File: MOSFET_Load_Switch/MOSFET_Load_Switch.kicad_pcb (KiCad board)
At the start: 4 copper layers, 44.2 x 16.5 mm, 18 parts, among them J1 PIN, J2 SW, J3 POUT, J4 PMOS_Socket, J5 PMOS_Plug, Q1 DMG2301L, Q2 DMG2301L

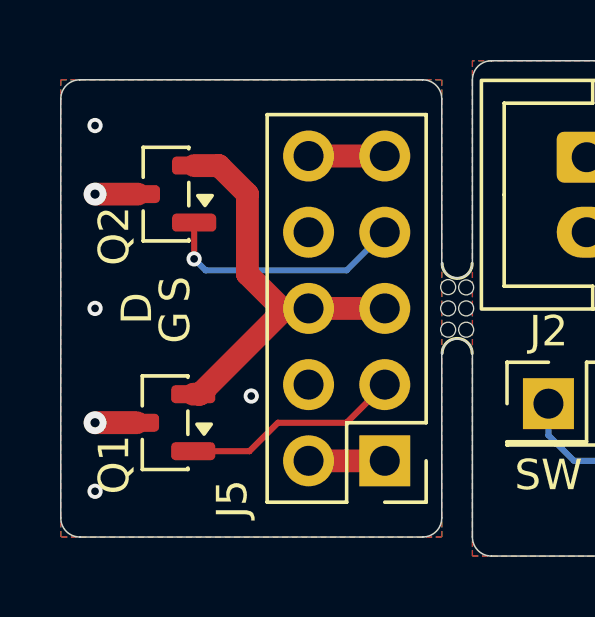
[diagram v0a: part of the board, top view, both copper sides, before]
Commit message: LED header sent to fab
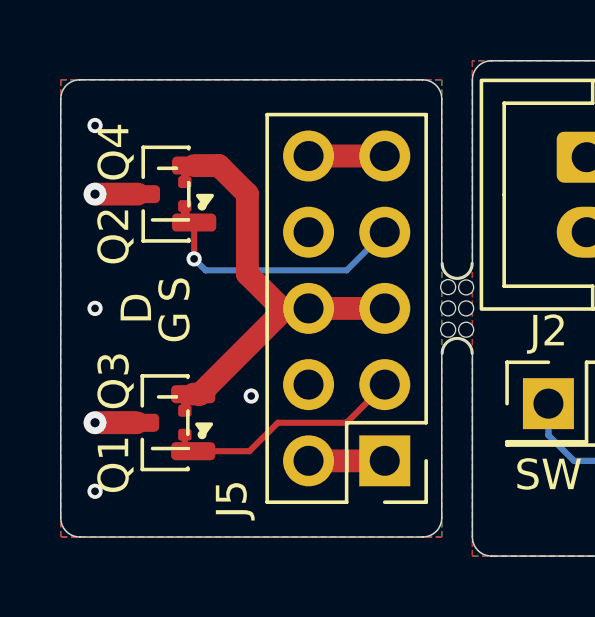
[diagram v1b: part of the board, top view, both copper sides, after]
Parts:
- removed mouse-bite-1mm-3mm: VAL**, ProjectLibrary:mouse-bite-1mm-3mm
- added B1: MouseBite, ProjectLibrary:mouse-bite-1mm-3mm, F.Cu at (113.8, 99.7)
- added Q3: DMG2301L, Package_TO_SOT_SMD:SOT-723, F.Cu at (104.1, 103.5)
- added Q4: DMG2301L, Package_TO_SOT_SMD:SOT-723, F.Cu at (104.1, 95.9)
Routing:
- net /VS: track 31.1 -> 32.4 mm
- net /VG2: track 12.2 -> 12.9 mm
- net /VG1: track 14.1 -> 14.8 mm
